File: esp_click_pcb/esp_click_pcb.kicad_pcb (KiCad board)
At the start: 2 copper layers, 90 x 60 mm, 52 parts, among them J1 USB_C, SW1 BOOT, SW2 FLASH, SW3 BT1, SW4 BT2, SW5 BT3, SW6 BT4, U1 ESP32-C6-MINI, U2 HT7833, U4 BQ24075

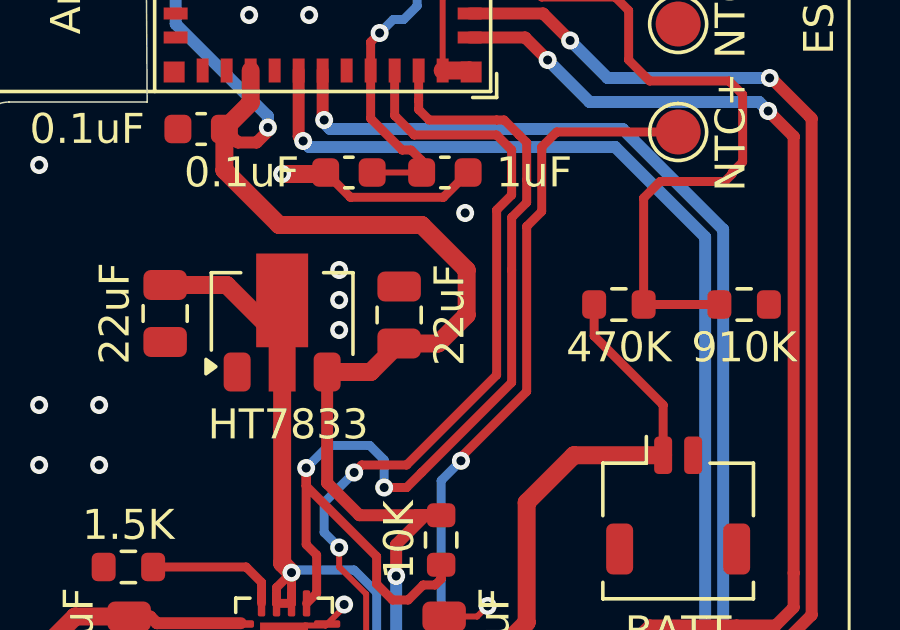
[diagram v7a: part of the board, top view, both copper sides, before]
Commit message: update cap value
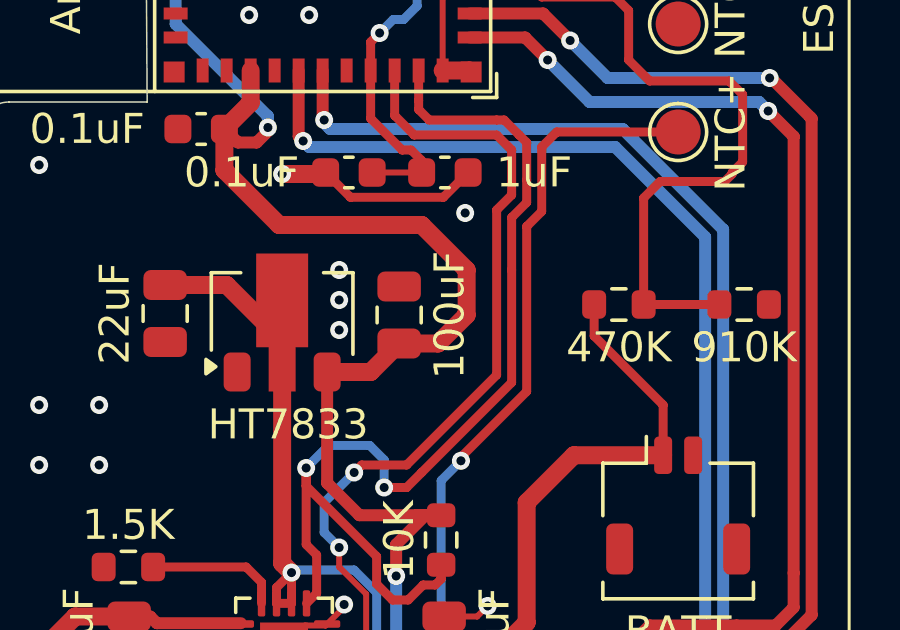
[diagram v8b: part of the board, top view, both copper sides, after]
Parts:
- C1: value 22uF -> 100uF
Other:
- board text added: "REV 4 - 2026 MADHUKAR TEMBA"
- board text removed: "REV 3 - 2026 MADHUKAR TEMBA"
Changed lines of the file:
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@@
 	(title_block
 		(title "ESP Click")
-		(date "2026-03-14")
-		(rev "3")
+		(date "2026-03-19")
+		(rev "4")
 		(company "Madhukar Temba")
 	)
@@
 			)
 		)
-		(property "Value" "22uF"
+		(property "Value" "100uF"
 			(at 0 1.68 90)
 			(layer "F.SilkS")
@@
 		)
 	)
-	(gr_text "REV 3 - 2026\nMADHUKAR TEMBA"
+	(gr_text "REV 4 - 2026\nMADHUKAR TEMBA"
 		(at 189 125 0)
 		(layer "B.SilkS")
@@
 			(justify left bottom mirror)
 		)
-		(render_cache "REV 3 - 2026\nMADHUKAR TEMBA" 0
+		(render_cache "REV 4 - 2026\nMADHUKAR TEMBA" 0
 			(polygon
 				(pts
@@
 			(polygon
 				(pts
-					(xy 177.385153 118.587761) (xy 177.396837 118.747561) (xy 177.430238 118.887084) (xy 177.483888 119.00963)
-					(xy 177.598221 119.172761) (xy 177.741992 119.303271) (xy 177.91025 119.403428) (xy 178.100846 119.475279)
-					(xy 178.301929 119.517894) (xy 178.505861 119.532065) (xy 178.705346 119.520547) (xy 178.898421 119.48627)
-					(xy 179.082382 119.428072) (xy 179.24665 119.347051) (xy 179.393572 119.240414) (xy 179.521606 119.105983)
-					(xy 179.622793 118.946) (xy 179.697827 118.748595) (xy 179.043135 118.576404) (xy 178.980241 118.712593)
-					(xy 178.870943 118.834691) (xy 178.778673 118.895312) (xy 178.669626 118.93271) (xy 178.539384 118.945882)
-					(xy 178.386243 118.924816) (xy 178.312218 118.897527) (xy 178.247758 118.859237) (xy 178.192585 118.808494)
-					(xy 178.147008 118.742916) (xy 178.11771 118.665482) (xy 178.107074 118.565413) (xy 178.120938 118.458112)
-					(xy 178.159647 118.375087) (xy 178.220072 118.307193) (xy 178.298133 118.254553) (xy 178.388205 118.217083)
-					(xy 178.493222 118.191172) (xy 178.711392 118.172121) (xy 178.900436 118.172121) (xy 178.900436 117.65628)
-					(xy 178.694722 117.65628) (xy 178.501648 117.641625) (xy 178.412905 117.620275) (xy 178.335868 117.587037)
-					(xy 178.269483 117.54005) (xy 178.218449 117.480059) (xy 178.186228 117.405812) (xy 178.174302 117.303654)
-					(xy 178.187669 117.203115) (xy 178.225371 117.123738) (xy 178.287691 117.060389) (xy 178.408656 116.997545)
-					(xy 178.54781 116.976308) (xy 178.645343 116.986611) (xy 178.731955 117.016635) (xy 178.810127 117.066617)
-					(xy 178.87511 117.132814) (xy 178.923174 117.212386) (xy 178.954841 117.307868) (xy 179.609717 117.156742)
-					(xy 179.54047 116.97799) (xy 179.445952 116.827564) (xy 179.326694 116.698473) (xy 179.187848 116.592725)
-					(xy 179.032784 116.51009) (xy 178.8627 116.450026) (xy 178.684445 116.413921) (xy 178.501648 116.401849)
-					(xy 178.306552 116.414504) (xy 178.117698 116.452224) (xy 177.93943 116.516902) (xy 177.783941 116.607562)
-					(xy 177.651296 116.725408) (xy 177.546903 116.869696) (xy 177.497747 116.977838) (xy 177.467244 117.100572)
-					(xy 177.456594 117.240823) (xy 177.472984 117.40084) (xy 177.520068 117.53849) (xy 177.597278 117.658478)
-					(xy 177.699504 117.759274) (xy 177.818162 117.834989) (xy 177.955949 117.886906) (xy 177.955949 117.899546)
-					(xy 177.834701 117.938086) (xy 177.725139 117.994068) (xy 177.627026 118.065868) (xy 177.544705 118.149406)
-					(xy 177.477547 118.244678) (xy 177.427102 118.350724) (xy 177.395786 118.464755)
+					(xy 179.727137 118.283862) (xy 179.727137 118.87554) (xy 178.32964 118.87554) (xy 178.32964 119.45)
+					(xy 177.670551 119.45) (xy 177.670551 118.87554) (xy 177.26352 118.87554) (xy 177.26352 118.301081)
+					(xy 177.674764 118.301081) (xy 178.325427 118.301081) (xy 179.043135 118.301081) (xy 178.337883 117.204553)
+					(xy 178.325427 117.204553) (xy 178.325427 118.301081) (xy 177.674764 118.301081) (xy 177.674764 116.483914)
+					(xy 178.518501 116.483914)
 				)
 			)
